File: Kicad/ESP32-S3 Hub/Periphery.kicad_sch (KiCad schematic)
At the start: 12 parts, among them SW1 KMR2, SW2 KMR2, SW3 DS04-254-2-04BK-SMT, U2 74HC595, U4 SP3485EN

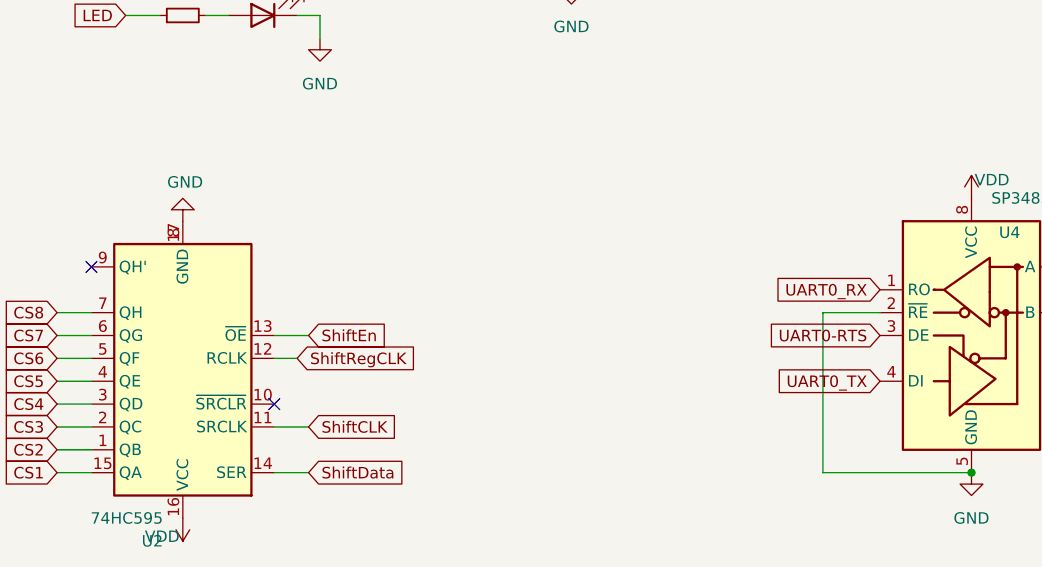
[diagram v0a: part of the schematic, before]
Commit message: Fixed ERC errors, stopped tracking a few .obsidian files
The only errors that popped up were the dual labeling of CS0 and Uart RTS, a power flag spot, and a modified footprint error.
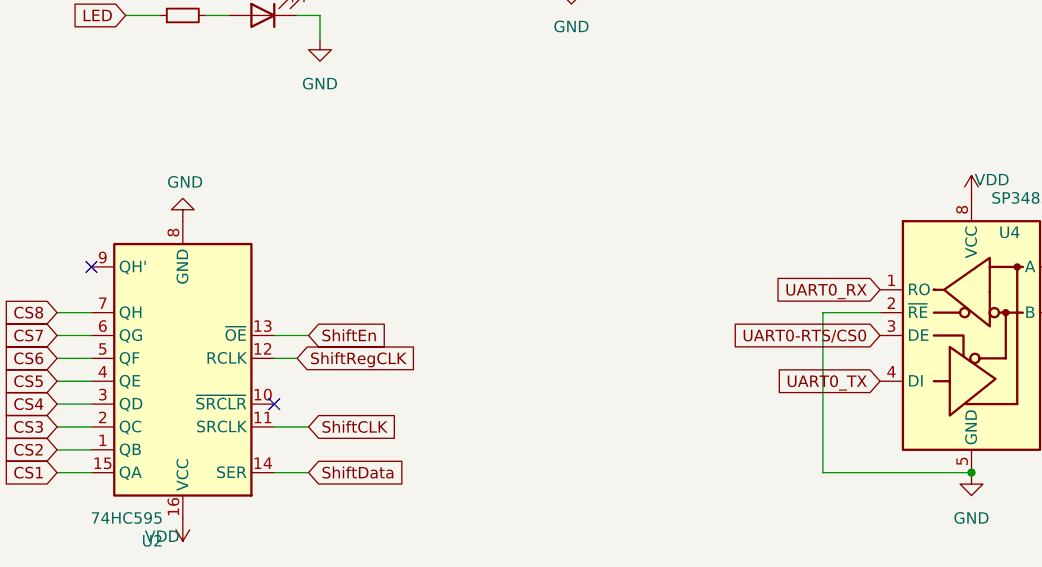
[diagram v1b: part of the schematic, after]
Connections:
- net GND: no longer U2.17 (GND)
- net UART0-RTS renamed UART0-RTS/CS0
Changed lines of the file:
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@@
-		)
-	)
-	(global_label "UART0-RTS"
-		(shape input)
-		(at 134.62 86.36 180)
-		(fields_autoplaced yes)
-		(effects
-			(font
-				(size 1.27 1.27)
-			)
-			(justify right)
-		)
-		(property "Intersheetrefs" "${INTERSHEET_REFS}"
-			(at 120.7491 86.36 0)
-			(effects
-				(font
-					(size 1.27 1.27)
-				)
-				(justify right)
-				(hide yes)
-			)
 		)
 	)
@@
 				)
 				(justify left)
+				(hide yes)
+			)
+		)
+	)
+	(global_label "UART0-RTS{slash}CS0"
+		(shape input)
+		(at 134.62 86.36 180)
+		(fields_autoplaced yes)
+		(effects
+			(font
+				(size 1.27 1.27)
+			)
+			(justify right)
+		)
+		(property "Intersheetrefs" "${INTERSHEET_REFS}"
+			(at 115.7296 86.36 0)
+			(effects
+				(font
+					(size 1.27 1.27)
+				)
+				(justify right)
 				(hide yes)
 			)
@@
 		(pin "10"
 		)
-		(pin "17"
-		)
 		(instances

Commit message: Switched out Mezzanine Connectors
I'm going with some 30-pin TE mezzanine connectors, which are cheaper than before and have a few extra pins if I need them in the future.
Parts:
- SW3: footprint (none) -> Button_Switch_SMD:SW_DIP_SPSTx04_Slide_Omron_A6S-410x_W8.9mm_P2.54mm
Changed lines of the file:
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@@
 			)
 		)
-		(property "Footprint" ""
+		(property "Footprint" "Button_Switch_SMD:SW_DIP_SPSTx04_Slide_Omron_A6S-410x_W8.9mm_P2.54mm"
 			(at 193.04 110.49 0)
 			(effects

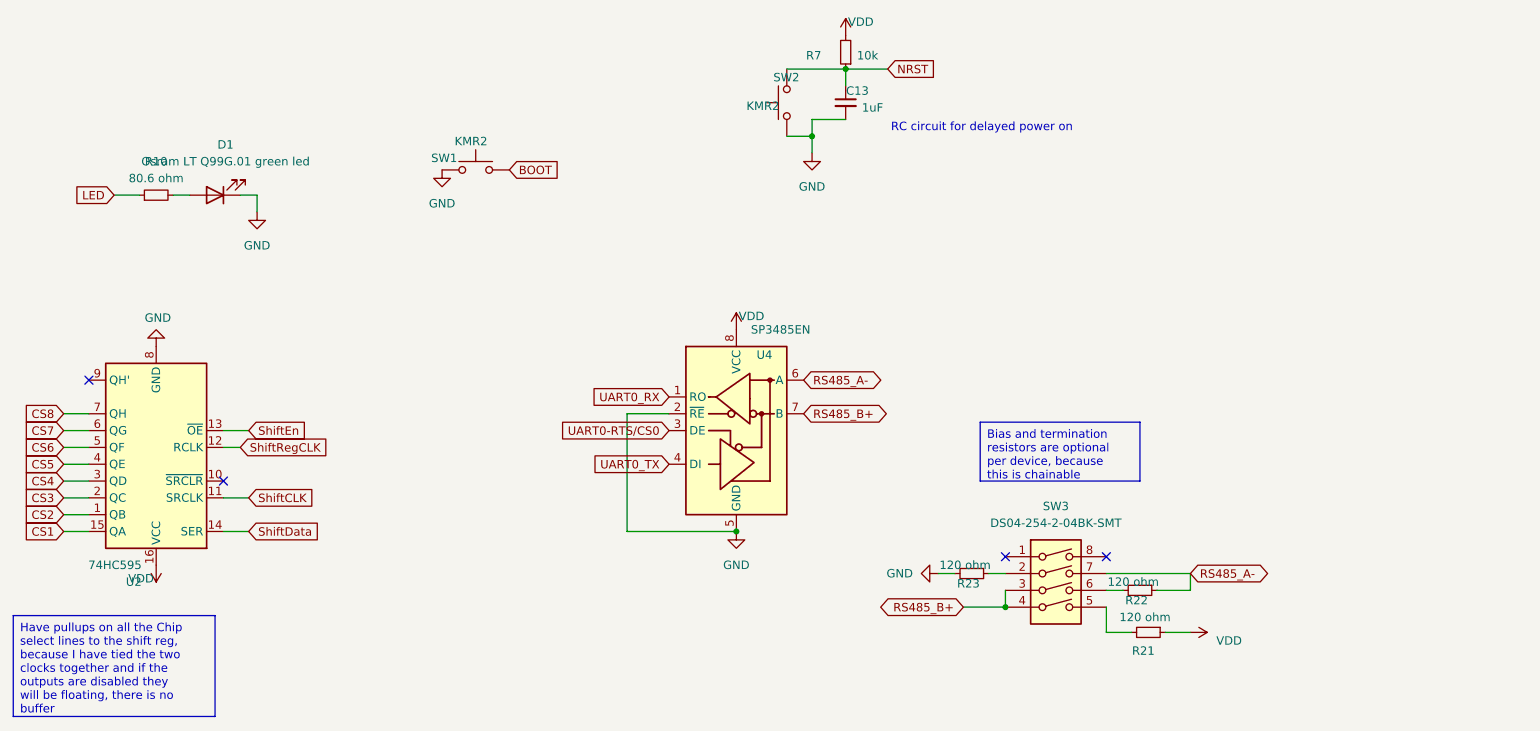
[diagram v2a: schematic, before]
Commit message: Switching out footprints for smaller variants, dropping rs485 resistors
Space is tight, so I had to downsize the crystal and the reset switches. I also don't have space for the rs485 termination resistors configurable per device, so I have excluded this from the board.
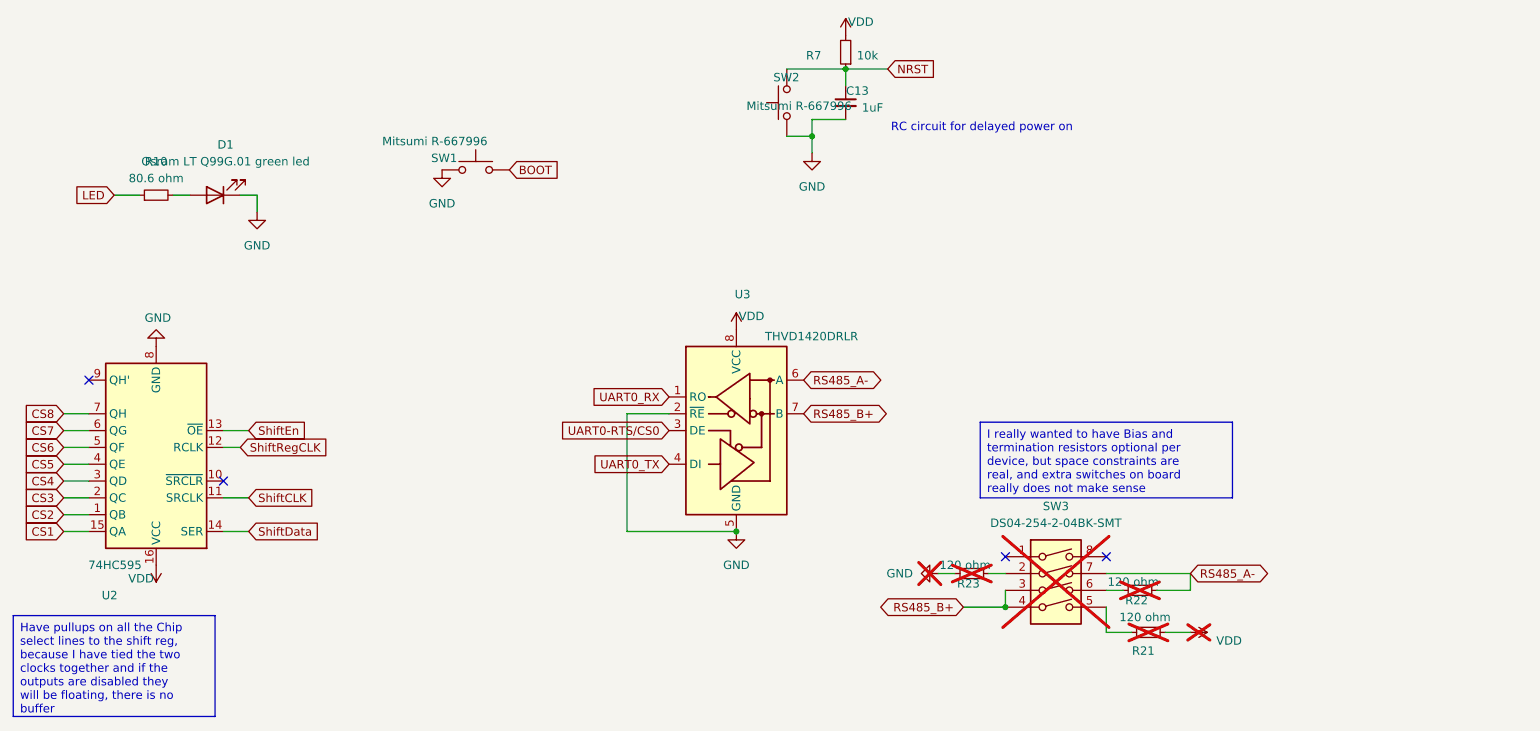
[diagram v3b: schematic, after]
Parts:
- removed U4: SP3485EN, Package_SO:SOIC-8_3.9x4.9mm_P1.27mm, symbol Interface_UART:SP3485EN
- added U3: THVD1420DRLR, Package_TO_SOT_SMD:SOT-583-8, symbol Interface_UART:THVD1420D
- C13: footprint Capacitor_SMD:C_0603_1608Metric_Pad1.08x0.95mm_HandSolder -> Capacitor_SMD:C_0402_1005Metric
- R10, R7: footprint Resistor_SMD:R_0603_1608Metric -> Resistor_SMD:R_0402_1005Metric
- R21, R22, R23: footprint Resistor_SMD:R_0603_1608Metric -> Resistor_SMD:R_0402_1005Metric; now not fitted; now left out of the parts list
- SW1, SW2: value KMR2 -> Mitsumi R-667996; footprint Button_Switch_SMD:SW_Push_1P1T_NO_CK_KMR2 -> Misumi switches:R-667995_MIT
- SW3: now not fitted; now left out of the parts list
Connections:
- net GND: now also U2.17 (GND), U3.2 (~{RE}), U3.5 (GND)
- net RS485_A-: now also U3.6 (A)
- net RS485_B+: now also U3.7 (B)
- net UART0-RTS/CS0: now also U3.3 (DE)
- net UART0_RX: now also U3.1 (RO)
- net UART0_TX: now also U3.4 (DI)
- net VDD: now also U3.8 (VCC)
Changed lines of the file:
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@@
+	)
+	(junction
+		(at 144.78 101.6)
+		(diameter 0)
+		(color 0 0 0 0)
 	)
 	(junction
@@
 		(color 0 0 0 0)
 	)
-	(junction
-		(at 144.78 101.6)
-		(diameter 0)
-		(color 0 0 0 0)
-	)
 	(no_connect
 		(at 67.31 93.98)
@@
 		)
 	)
-	(text_box "Bias and termination resistors are optional per device, because this is chainable"
+	(text_box "I really wanted to have Bias and termination resistors optional per device, but space constraints are real, and extra switches on board really does not make sense"
 		(exclude_from_sim no)
 		(at 181.61 85.09 0)
-		(size 24.13 8.89)
+		(size 38.1 11.43)
 		(stroke
 			(width 0)
@@
 		(on_board yes)
 		(dnp no)
-		(fields_autoplaced yes)
 		(property "Reference" "U2"
-			(at 54.9559 109.22 0)
+			(at 51.308 111.252 0)
 			(effects
 				(font
@@
 		)
 		(pin "10"
+		)
+		(pin "17"
 		)
 		(instances
@@
 		(at 180.34 107.95 270)
 		(unit 1)
-		(exclude_from_sim no)
-		(in_bom yes)
-		(on_board yes)
-		(dnp no)
+		(exclude_from_sim yes)
+		(in_bom no)
+		(on_board no)
+		(dnp yes)
 		(property "Reference" "R23"
 			(at 179.832 109.474 90)
@@
 			)
 		)
-		(property "Footprint" "Resistor_SMD:R_0603_1608Metric"
+		(property "Footprint" "Resistor_SMD:R_0402_1005Metric"
 			(at 180.34 107.95 0)
 			(effects
@@
 			)
 		)
-		(property "Value" "KMR2"
+		(property "Value" "Mitsumi R-667996"
 			(at 146.304 37.338 90)
 			(effects
@@
 			)
 		)
-		(property "Footprint" "Button_Switch_SMD:SW_Push_1P1T_NO_CK_KMR2"
+		(property "Footprint" "Misumi switches:R-667995_MIT"
 			(at 147.32 36.83 0)
 			(effects
@@
 				(path "/a8c80fba-3bca-4358-b5bb-9ebf9383c658/c12991ca-4617-4c32-8678-9934d12b2f96"
 					(reference "SW2")
+					(unit 1)
+				)
+			)
+		)
+	)
+	(symbol
+		(lib_id "Interface_UART:THVD1420D")
+		(at 144.78 86.36 0)
+		(unit 1)
+		(exclude_from_sim no)
+		(in_bom yes)
+		(on_board yes)
+		(dnp no)
+		(property "Reference" "U3"
+			(at 144.526 65.786 0)
+			(effects
+				(font
+					(size 1.27 1.27)
+				)
+				(justify left)
+			)
+		)
+		(property "Value" "THVD1420DRLR"
+			(at 149.098 72.136 0)
+			(effects
+				(font
+					(size 1.27 1.27)
+				)
+				(justify left)
+			)
+		)
+		(property "Footprint" "Package_TO_SOT_SMD:SOT-583-8"
+			(at 144.78 104.14 0)
+			(effects
+				(font
+					(size 1.27 1.27)
+				)
+				(hide yes)
+			)
+		)
+		(property "Datasheet" "https://www.ti.com/lit/ds/symlink/thvd1420.pdf"
+			(at 144.78 85.09 0)
+			(effects
+				(font
+					(size 1.27 1.27)
+				)
+				(hide yes)
+			)
+		)
+		(property "Description" "Half duplex RS-485/RS-422, 12 Mbps, 3V - 5.5V supply, ±12kV electro-static discharge (ESD) protection, with receiver/driver enable, 32 receiver drive capacity, SOIC-8"
+			(at 144.78 86.36 0)
+			(effects
+				(font
+					(size 1.27 1.27)
+				)
+				(hide yes)
+			)
+		)
+		(pin "3"
+		)
+		(pin "1"
+		)
+		(pin "4"
+		)
+		(pin "2"
+		)
+		(pin "7"
+		)
+		(pin "8"
+		)
+		(pin "6"
+		)
+		(pin "5"
+		)
+		(instances
+			(project ""
+				(path "/a8c80fba-3bca-4358-b5bb-9ebf9383c658/c12991ca-4617-4c32-8678-9934d12b2f96"
+					(reference "U3")
 					(unit 1)
 				)
@@
 			)
 		)
-		(property "Value" "KMR2"
+		(property "Value" "Mitsumi R-667996"
 			(at 107.188 42.672 0)
 			(effects
@@
 			)
 		)
-		(property "Footprint" "Button_Switch_SMD:SW_Push_1P1T_NO_CK_KMR2"
+		(property "Footprint" "Misumi switches:R-667995_MIT"
 			(at 105.41 41.91 0)
 			(effects
@@
 			)
 		)
-		(property "Footprint" "Resistor_SMD:R_0603_1608Metric"
+		(property "Footprint" "Resistor_SMD:R_0402_1005Metric"
 			(at 161.29 29.21 0)
 			(effects
@@
 			)
 		)
-		(property "Footprint" "Resistor_SMD:R_0603_1608Metric"
+		(property "Footprint" "Resistor_SMD:R_0402_1005Metric"
 			(at 57.15 50.8 0)
 			(effects
@@
 		(at 175.26 107.95 270)
 		(unit 1)
-		(exclude_from_sim no)
-		(in_bom yes)
-		(on_board yes)
-		(dnp no)
+		(exclude_from_sim yes)
+		(in_bom no)
+		(on_board no)
+		(dnp yes)
 		(fields_autoplaced yes)
 		(property "Reference" "#PWR038"
@@
 				(path "/a8c80fba-3bca-4358-b5bb-9ebf9383c658/c12991ca-4617-4c32-8678-9934d12b2f96"
 					(reference "#PWR038")
-					(unit 1)
-				)
-			)
-		)
-	)
-	(symbol
-		(lib_id "Interface_UART:SP3485EN")
-		(at 144.78 86.36 0)
-		(unit 1)
-		(exclude_from_sim no)
-		(in_bom yes)
-		(on_board yes)
-		(dnp no)
-		(property "Reference" "U4"
-			(at 147.828 74.93 0)
-			(effects
-				(font
-					(size 1.27 1.27)
-				)
-				(justify left)
-			)
-		)
-		(property "Value" "SP3485EN"
-			(at 146.9741 71.12 0)
-			(effects
-				(font
-					(size 1.27 1.27)
-				)
-				(justify left)
-			)
-		)
-		(property "Footprint" "Package_SO:SOIC-8_3.9x4.9mm_P1.27mm"
-			(at 171.45 95.25 0)
-			(effects
-				(font
-					(size 1.27 1.27)
-					(italic yes)
-				)
-				(hide yes)
-			)
-		)
-		(property "Datasheet" "http://www.icbase.com/pdf/SPX/SPX00480106.pdf"
-			(at 144.78 86.36 0)
-			(effects
-				(font
-					(size 1.27 1.27)
-				)
-				(hide yes)
-			)
-		)
-		(property "Description" "Industrial 3.3V Low Power Half-Duplex RS-485 Transceiver 10Mbps, SOIC-8"
-			(at 144.78 86.36 0)
-			(effects
-				(font
-					(size 1.27 1.27)
-				)
-				(hide yes)
-			)
-		)
-		(pin "1"
-		)
-		(pin "7"
-		)
-		(pin "3"
-		)
-		(pin "6"
-		)
-		(pin "8"
-		)
-		(pin "4"
-		)
-		(pin "5"
-		)
-		(pin "2"
-		)
-		(instances
-			(project ""
-				(path "/a8c80fba-3bca-4358-b5bb-9ebf9383c658/c12991ca-4617-4c32-8678-9934d12b2f96"
-					(reference "U4")
 					(unit 1)
 				)
@@
 			)
 		)
-		(property "Footprint" "Capacitor_SMD:C_0603_1608Metric_Pad1.08x0.95mm_HandSolder"
+		(property "Footprint" "Capacitor_SMD:C_0402_1005Metric"
 			(at 161.29 36.83 0)
 			(effects
@@
 		(at 213.36 116.84 270)
 		(unit 1)
-		(exclude_from_sim no)
-		(in_bom yes)
-		(on_board yes)
-		(dnp no)
+		(exclude_from_sim yes)
+		(in_bom no)
+		(on_board no)
+		(dnp yes)
 		(property "Reference" "#PWR037"
 			(at 209.55 116.84 0)
@@
 		(at 193.04 110.49 0)
 		(unit 1)
-		(exclude_from_sim no)
-		(in_bom yes)
-		(on_board yes)
-		(dnp no)
+		(exclude_from_sim yes)
+		(in_bom no)
+		(on_board no)
+		(dnp yes)
 		(fields_autoplaced yes)
 		(property "Reference" "SW3"
@@
 		(at 207.01 116.84 270)
 		(unit 1)
-		(exclude_from_sim no)
-		(in_bom yes)
-		(on_board yes)
-		(dnp no)
+		(exclude_from_sim yes)
+		(in_bom no)
+		(on_board no)
+		(dnp yes)
 		(property "Reference" "R21"
 			(at 206.248 119.634 90)
@@
 			)
 		)
-		(property "Footprint" "Resistor_SMD:R_0603_1608Metric"
+		(property "Footprint" "Resistor_SMD:R_0402_1005Metric"
 			(at 207.01 116.84 0)
 			(effects
@@
 		(at 205.74 110.49 270)
 		(unit 1)
-		(exclude_from_sim no)
-		(in_bom yes)
-		(on_board yes)
-		(dnp no)
+		(exclude_from_sim yes)
+		(in_bom no)
+		(on_board no)
+		(dnp yes)
 		(property "Reference" "R22"
 			(at 205.232 112.014 90)
@@
 			)
 		)
-		(property "Footprint" "Resistor_SMD:R_0603_1608Metric"
+		(property "Footprint" "Resistor_SMD:R_0402_1005Metric"
 			(at 205.74 110.49 0)
 			(effects

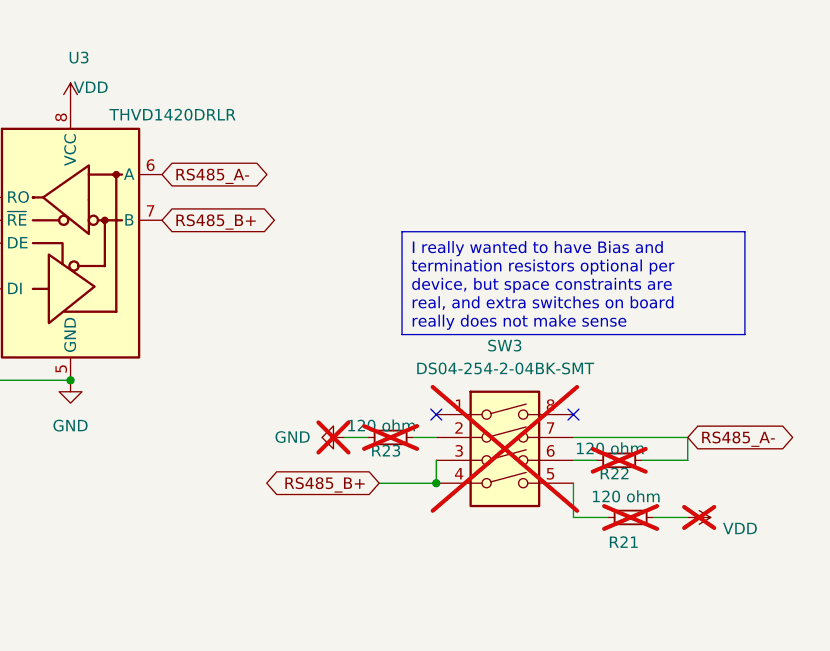
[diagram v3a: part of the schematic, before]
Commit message: Swapping register pins
I tryid to simplify the layout a little bit. I also added a note about the potential danger of the i2c lines on low level glitching pins.
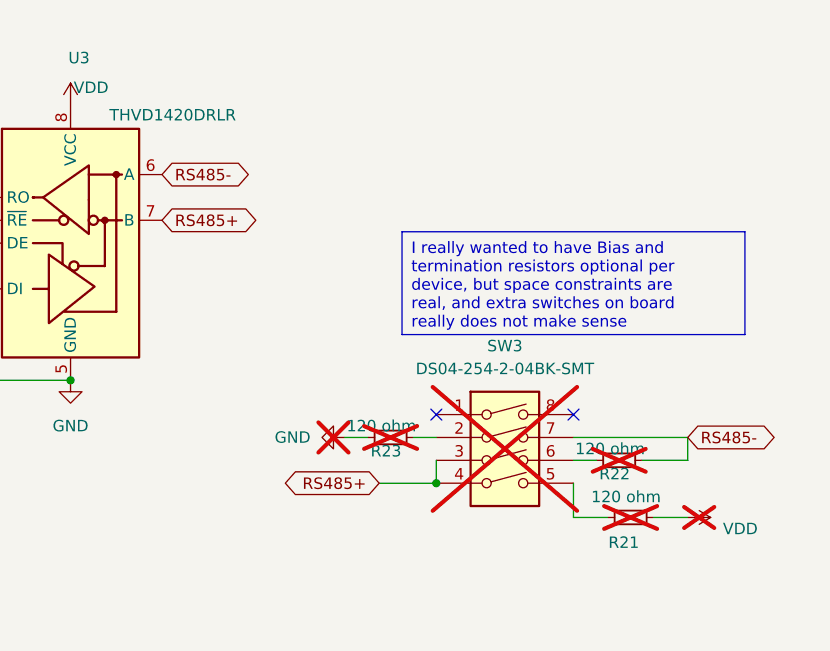
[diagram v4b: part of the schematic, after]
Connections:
- net RS485_A- renamed RS485-
- net RS485_B+ renamed RS485+
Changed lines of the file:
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@@
 		)
 	)
-	(global_label "RS485_B+"
+	(global_label "RS485+"
 		(shape bidirectional)
 		(at 179.07 113.03 180)
@@
 		)
 		(property "Intersheetrefs" "${INTERSHEET_REFS}"
-			(at 165.0555 113.03 0)
+			(at 167.2931 113.03 0)
 			(effects
 				(font
@@
 		)
 	)
-	(global_label "RS485_B+"
+	(global_label "RS485+"
 		(shape bidirectional)
 		(at 154.94 83.82 0)
@@
 		)
 		(property "Intersheetrefs" "${INTERSHEET_REFS}"
-			(at 168.9545 83.82 0)
+			(at 166.7169 83.82 0)
 			(effects
 				(font
@@
 		)
 	)
-	(global_label "RS485_A-"
+	(global_label "RS485-"
 		(shape bidirectional)
 		(at 154.94 78.74 0)
@@
 		)
 		(property "Intersheetrefs" "${INTERSHEET_REFS}"
-			(at 168.7731 78.74 0)
-			(effects
-				(font
-					(size 1.27 1.27)
-				)
-				(justify left)
-				(hide yes)
-			)
-		)
-	)
-	(global_label "RS485_A-"
+			(at 166.7169 78.74 0)
+			(effects
+				(font
+					(size 1.27 1.27)
+				)
+				(justify left)
+				(hide yes)
+			)
+		)
+	)
+	(global_label "RS485-"
 		(shape bidirectional)
 		(at 213.36 107.95 0)
@@
 		)
 		(property "Intersheetrefs" "${INTERSHEET_REFS}"
-			(at 227.1931 107.95 0)
-			(effects
-				(font
+			(at 225.1369 107.95 0)
+			(effects
+				(font
